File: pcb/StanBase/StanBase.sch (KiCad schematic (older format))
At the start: 3 parts

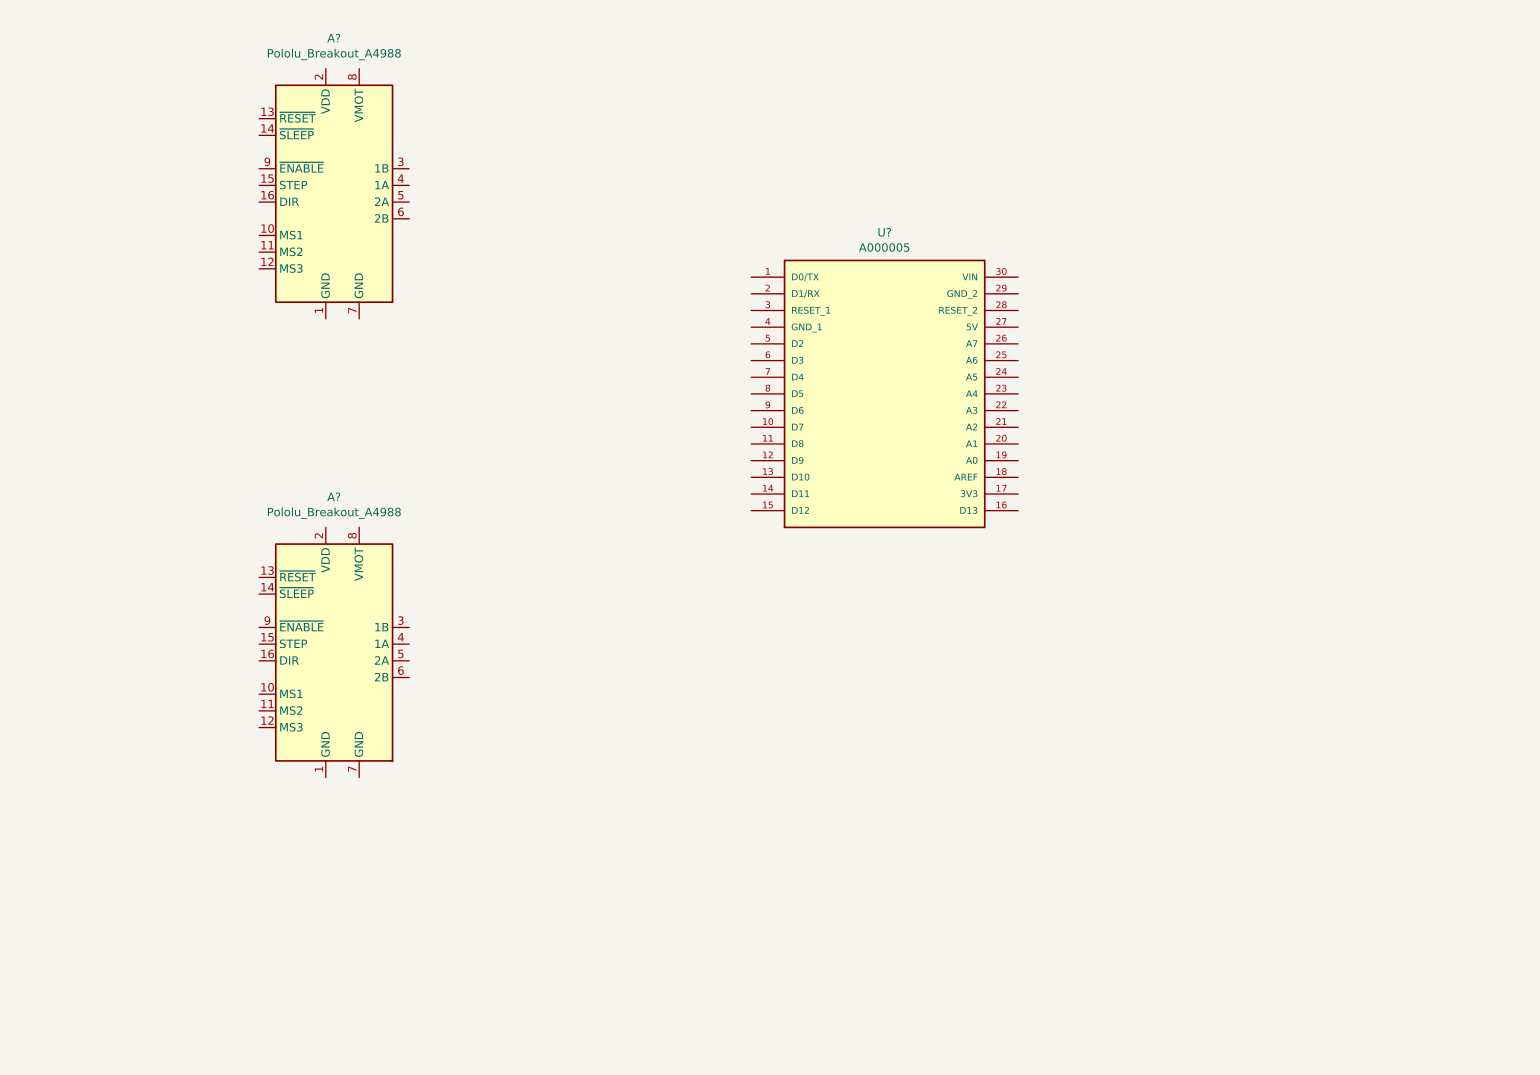
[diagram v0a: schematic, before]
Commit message: Added more components for PCB design
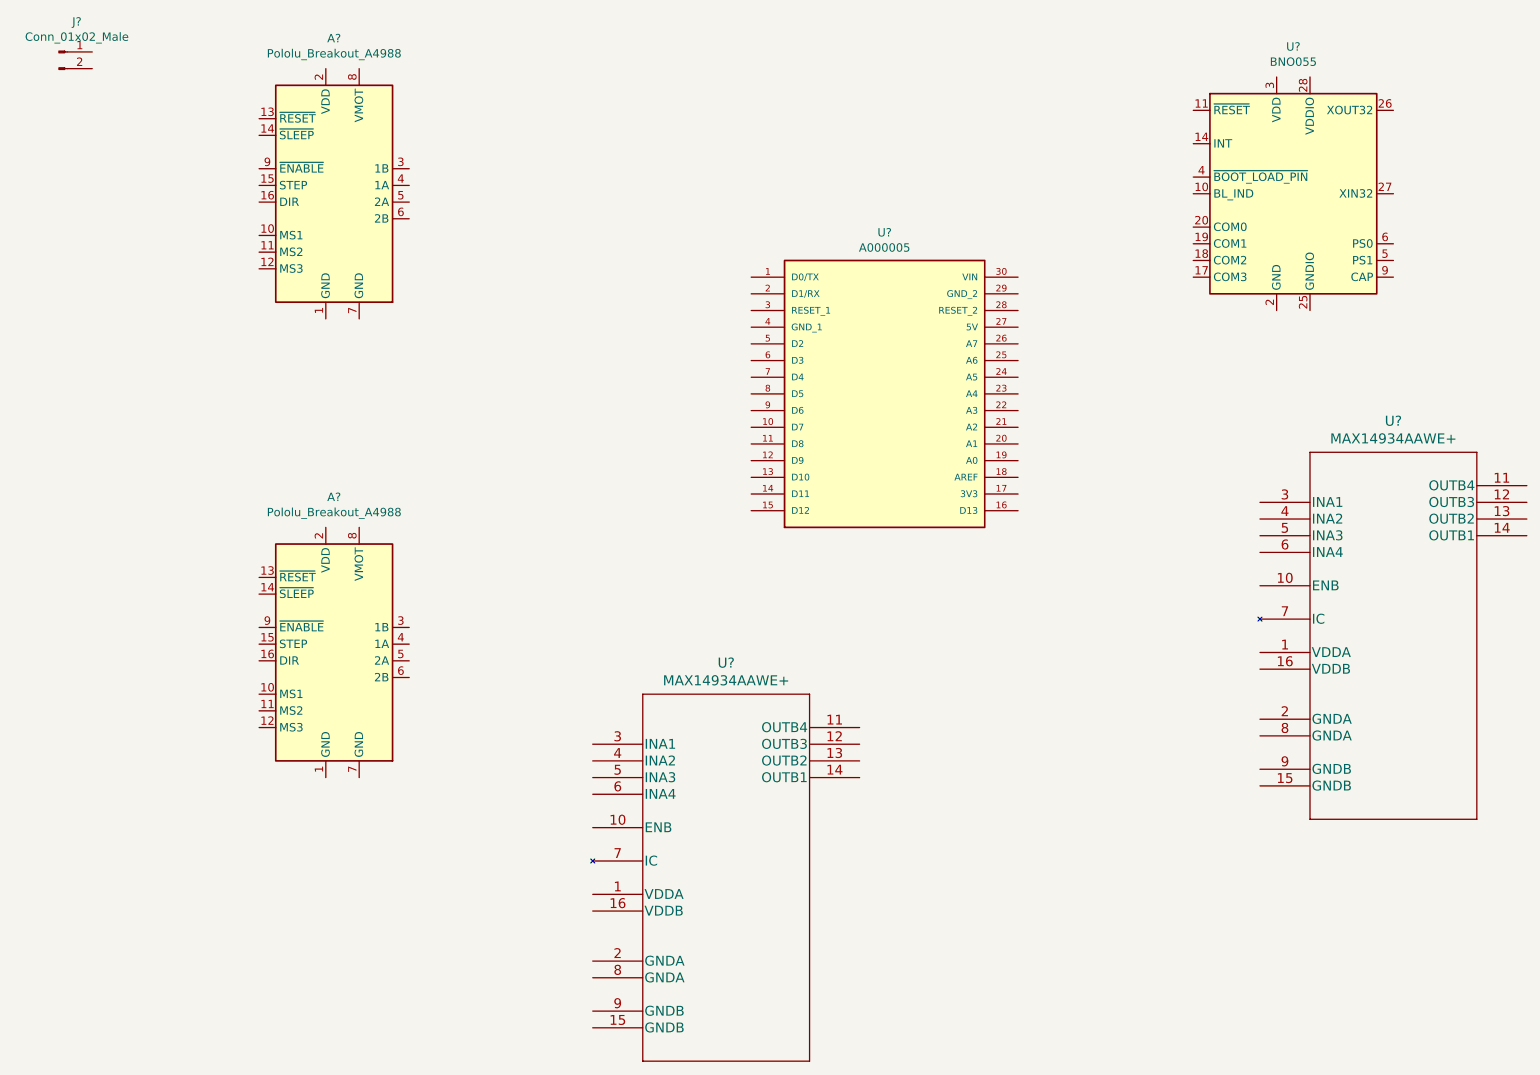
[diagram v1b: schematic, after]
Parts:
- added J?: Conn_01x02_Male, symbol Connector:Conn_01x02_Male
- added U?: BNO055, Package_LGA:LGA-28_5.2x3.8mm_P0.5mm, symbol Sensor_Motion:BNO055
- added U? (x2): MAX14934AAWE+, 21-0042B_16_MXM, symbol 2021-05-23_10-52-06:MAX14934AAWE+
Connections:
- new net: U?.15 (GNDIO), U?.16 (GNDIO), U?.25 (GNDIO)
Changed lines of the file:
@@
+	1    0    0    -1
+$EndComp
+$Comp
+L Sensor_Motion:BNO055 U?
+U 1 1 60AA352F
+P 8500 2250
+F 0 "U?" H 8500 3131 50  0000 C CNN
+F 1 "BNO055" H 8500 3040 50  0000 C CNN
+F 2 "Package_LGA:LGA-28_5.2x3.8mm_P0.5mm" H 8750 1600 50  0001 L CNN
+F 3 "https://ae-bst.resource.bosch.com/media/_tech/media/datasheets/BST_BNO055_DS000_14.pdf" H 8500 2450 50  0001 C CNN
+	1    8500 2250
+	1    0    0    -1
+$EndComp
+$Comp
+L 2021-05-23_10-52-06:MAX14934AAWE+ U?
+U 1 1 60AA5A98
+P 8300 4100
+F 0 "U?" H 9100 4587 60  0000 C CNN
+F 1 "MAX14934AAWE+" H 9100 4481 60  0000 C CNN
+F 2 "21-0042B_16_MXM" H 9100 4440 60  0001 C CNN
+F 3 "" H 8300 4100 60  0000 C CNN
+	1    8300 4100
+	1    0    0    -1
+$EndComp
+$Comp
+L 2021-05-23_10-52-06:MAX14934AAWE+ U?
+U 1 1 60AA7265
+P 4300 5550
+F 0 "U?" H 5100 6037 60  0000 C CNN
+F 1 "MAX14934AAWE+" H 5100 5931 60  0000 C CNN
+F 2 "21-0042B_16_MXM" H 5100 5890 60  0001 C CNN
+F 3 "" H 4300 5550 60  0000 C CNN
+	1    4300 5550
+	1    0    0    -1
+$EndComp
+$Comp
+L Connector:Conn_01x02_Male J?
+U 1 1 60AA9243
+P 1100 1400
+F 0 "J?" H 1208 1581 50  0000 C CNN
+F 1 "Conn_01x02_Male" H 1208 1490 50  0000 C CNN
+F 2 "" H 1100 1400 50  0001 C CNN
+F 3 "~" H 1100 1400 50  0001 C CNN
+	1    1100 1400
 	1    0    0    -1
 $EndComp

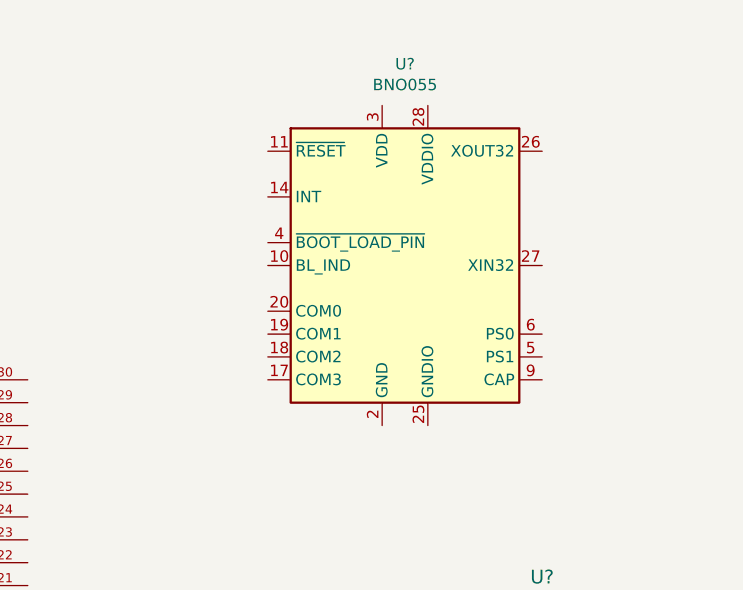
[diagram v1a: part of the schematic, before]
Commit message: Added project specific libraries
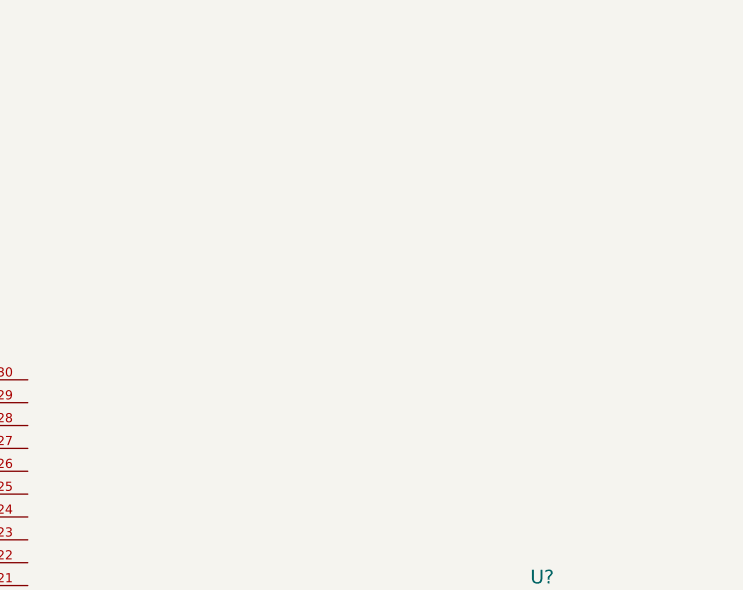
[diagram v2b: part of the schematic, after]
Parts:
- removed U?: BNO055, Package_LGA:LGA-28_5.2x3.8mm_P0.5mm, symbol Sensor_Motion:BNO055
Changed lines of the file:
@@
-$EndComp
-$Comp
-L Sensor_Motion:BNO055 U?
-U 1 1 60AA352F
-P 8500 2250
-F 0 "U?" H 8500 3131 50  0000 C CNN
-F 1 "BNO055" H 8500 3040 50  0000 C CNN
-F 2 "Package_LGA:LGA-28_5.2x3.8mm_P0.5mm" H 8750 1600 50  0001 L CNN
-F 3 "https://ae-bst.resource.bosch.com/media/_tech/media/datasheets/BST_BNO055_DS000_14.pdf" H 8500 2450 50  0001 C CNN
-	1    8500 2250
-	1    0    0    -1
 $EndComp
 $Comp
